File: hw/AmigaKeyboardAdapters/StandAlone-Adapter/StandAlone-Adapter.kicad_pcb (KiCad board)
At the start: 2 copper layers, 78.7 x 58.4 mm, 63 parts, among them J1 RJ10, J10 Conn_01x04, J11 Conn_01x02, J2 Conn_01x03, J3 Conn_02x03_Odd_Even, J4 Conn_01x04, J5 Conn_01x05, J6 Conn_01x03, J7 Conn_01x03, J8 Conn_01x02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

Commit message: New silkscreen (back) logo
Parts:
- added LOGO4: Stalker Logo, RetroBitLab:Stalker_16.1x17.3mm, B.Cu at (137.7, 110.8)

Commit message: First import for LCSC PCB Production and components placement
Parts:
- removed D2, D3: LED, LED_SMD:LED_1206_3216Metric_Pad1.42x1.75mm_HandSolder
- removed R2, R3: 1.5K, Resistor_SMD:R_1206_3216Metric_Pad1.30x1.75mm_HandSolder
- C1: value 10u -> 100nF; footprint Capacitor_Tantalum_SMD:CP_EIA-3216-12_Kemet-S_Pad1.58x1.35mm_HandSolder -> Capacitor_SMD:C_1206_3216Metric_Pad1.33x1.80mm_HandSolder
- C2: value 22u -> 10uF
- C7: value 4.7u -> 4.7uF
- C8, C9: value 20p -> 22pF
- D1, D4: value LED -> RED
- R1, R5: value 1.5K -> 330R
- R16, R17: value 12ohm -> 22R
- R4: value 22K -> 10K
- RESET1: footprint RetroBitLab:SW_SPST_FSMSM_3D -> RetroBitLab:SPST-7.3x3.9x2.5-WUERTH-434121025816
- USB1: value USB_A -> USB_A_SMD_LCSC; footprint RetroBitLab:CUI_UJ2-AH-4-TH -> RetroBitLab:USB_A_M04P-F000_LCSC_C386738
- XT1: footprint RetroBitLab:Crystal_HC49-4H_Vertical_3D -> Crystal:Crystal_SMD_HC49-SD
- moved LOGO3 9.19 mm to (167.9, 91.9)
- moved USB1 5.53 mm to (150.2, 83.0)
- moved C8 4.00 mm to (141.2, 87.8)
- moved C9 3.88 mm to (140.8, 100.8)
- moved XT1 1.93 mm to (135.6, 94.4)
- moved C14 1.39 mm to (157.8, 83.6)
- moved C12 1.11 mm to (159.5, 88.6)
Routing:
- net VCC3V3: track 250.0 -> 232.0 mm, vias 3 -> 1
- net KBD_CLOCK: track 66.8 -> 80.5 mm
- net NRST: track 41.7 -> 51.6 mm, vias 1 -> 0
- net VCC12V: track 8.37 -> 0.00 mm
- net KBD_DATA: track 56.9 -> 64.7 mm
- net Net-(D3-Pad2): track 6.95 -> 0.00 mm
- net Net-(R16-Pad2): track 18.8 -> 25.4 mm
- net Net-(C8-Pad1): track 21.8 -> 26.9 mm
- net Net-(R17-Pad2): track 18.3 -> 22.4 mm
- net Net-(C7-Pad1): track 14.2 -> 18.3 mm
- net Net-(D2-Pad1): track 4.03 -> 0.00 mm
- net Net-(D4-Pad1): track 16.5 -> 13.5 mm
- net Net-(C9-Pad1): track 16.3 -> 14.0 mm
- net Net-(R6-Pad1): track 46.7 -> 48.7 mm
- net +5V: track 162.8 -> 161.4 mm
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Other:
- board text added: "https://github.com/gianlucarenzi/stalker"

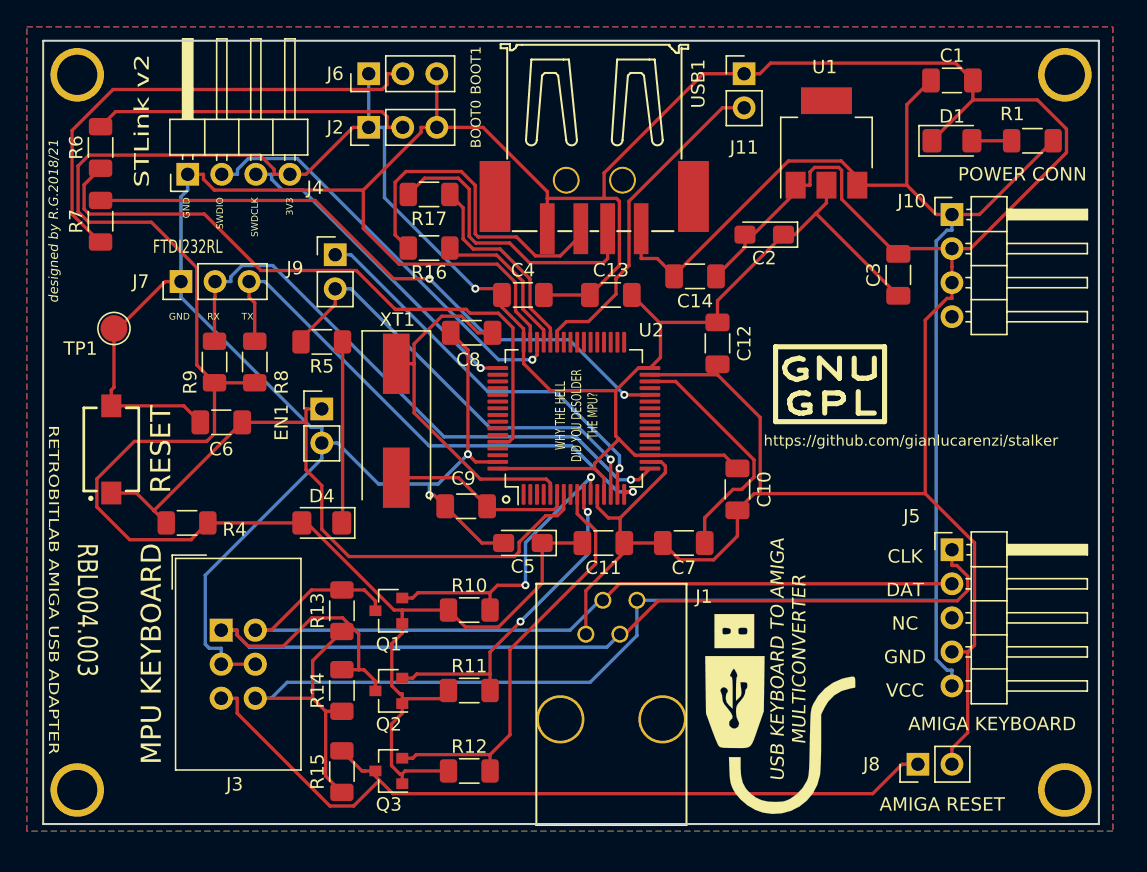
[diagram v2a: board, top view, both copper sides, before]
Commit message: All components are SMD for a easier PCB production (LCSC and others) The jumper headers are optionals, so it will be soldered if needed. The programming tool STLINK_V2 will have a special programming header male to match the connector on the board.
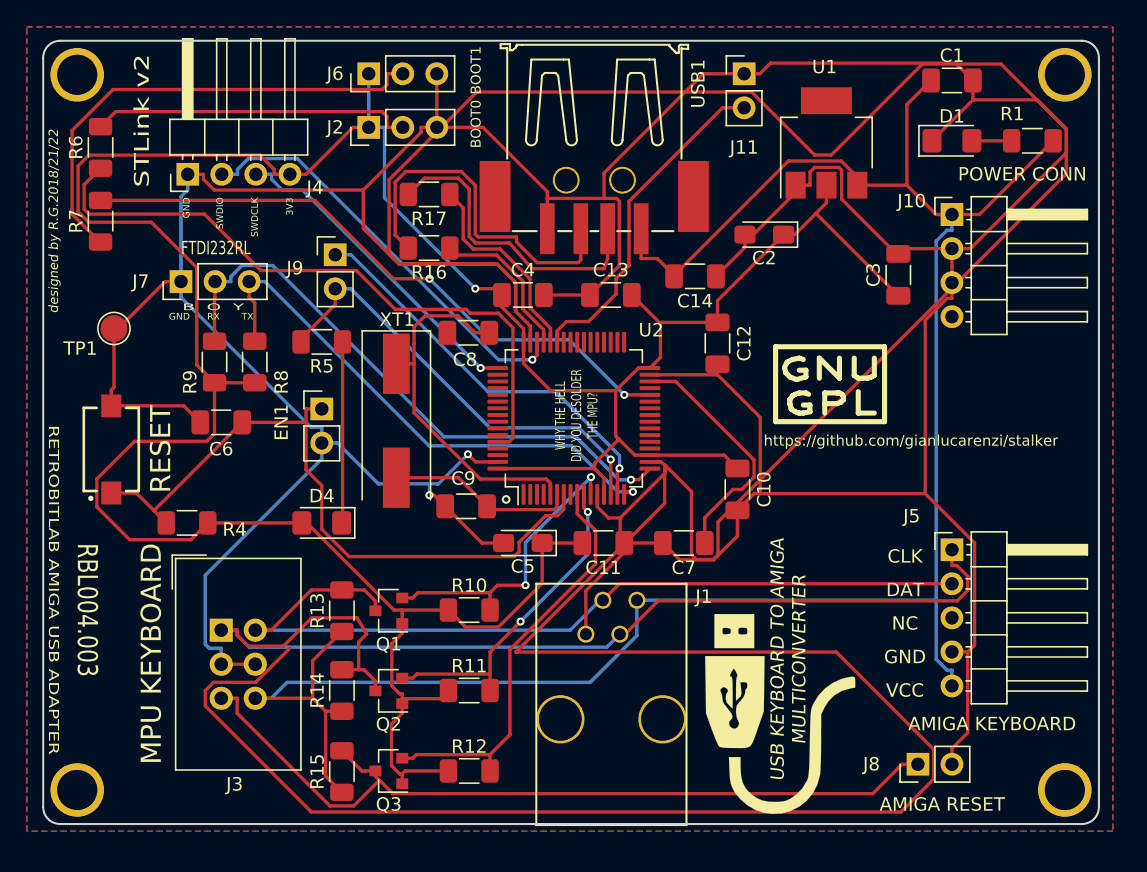
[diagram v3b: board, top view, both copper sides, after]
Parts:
- moved C8 0.25 mm to (140.9, 87.8)
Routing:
- net GND: track 368.8 -> 611.7 mm
- net Net-(R16-Pad2): track 25.4 -> 27.6 mm
- net KBD_CLOCK: track 80.5 -> 81.5 mm
- net Net-(R17-Pad2): track 22.4 -> 23.1 mm
- net Net-(C8-Pad1): track 26.9 -> 27.4 mm
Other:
- outline, holes or cut-outs redrawn
- board text added: "B O Y"
- board text added: "designed by R.G.2018/21/22"
- board text removed: "designed by R.G.2018/21"

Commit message: Sent to JLCPCB for quotes of 25 pcs and 100 pcs.
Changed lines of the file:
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@@
       (effects (font (size 0.8 0.8) (thickness 0.12)))
     )
-    (pad 1 smd roundrect (at -1.5625 0) (size 1.325 1.8) (layers F.Cu F.Paste F.Mask) (roundrect_rratio 0.1886784905660377)
+    (pad 1 smd roundrect (at -1.5625 0) (size 1.325 1.8) (layers F.Cu F.Paste F.Mask) (roundrect_rratio 0.1886777358490566)
       (net 6 +5V))
-    (pad 2 smd roundrect (at 1.5625 0) (size 1.325 1.8) (layers F.Cu F.Paste F.Mask) (roundrect_rratio 0.1886784905660377)
+    (pad 2 smd roundrect (at 1.5625 0) (size 1.325 1.8) (layers F.Cu F.Paste F.Mask) (roundrect_rratio 0.1886777358490566)
       (net 3 GND))
     (model ${KISYS3DMOD}/Capacitor_SMD.3dshapes/C_1206_3216Metric.wrl

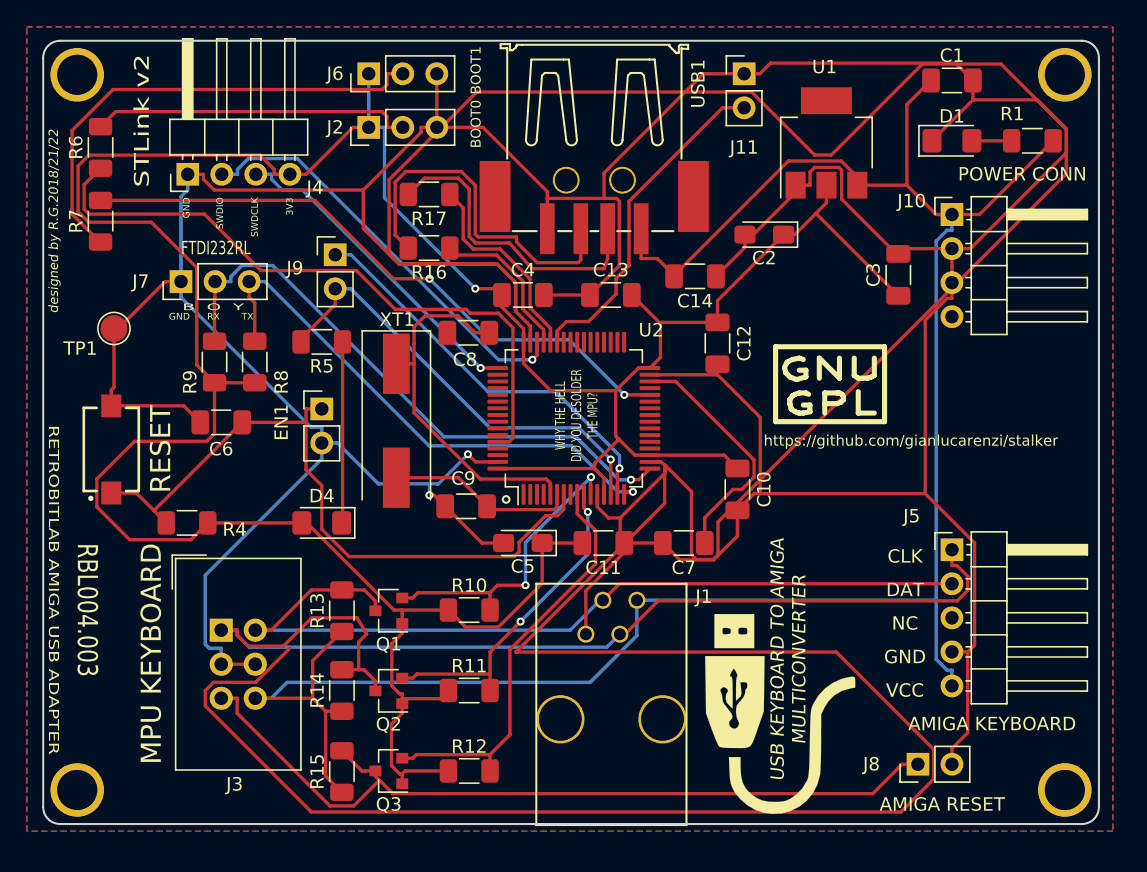
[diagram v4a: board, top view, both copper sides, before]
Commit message: Modified the JTAG STLinkV2 programmer port
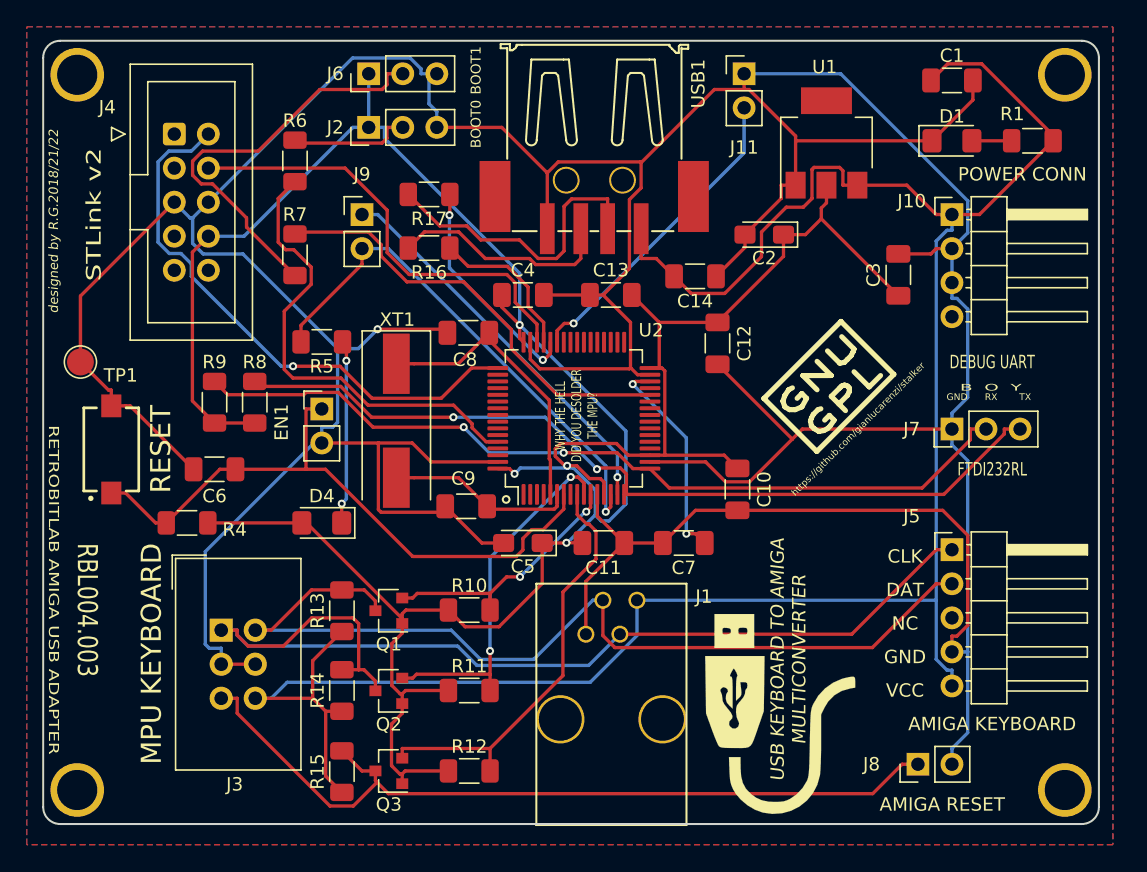
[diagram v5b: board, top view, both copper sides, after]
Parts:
- J4: value Conn_01x04 -> JTAG SWDIO SWCLK; footprint Connector_PinHeader_2.54mm:PinHeader_1x04_P2.54mm_Horizontal -> Connector_IDC:IDC-Header_2x05_P2.54mm_Vertical
- moved J7 58.5 mm to (177.0, 95.0)
- moved R7 14.7 mm to (128.0, 82.0)
- moved R6 14.5 mm to (128.0, 75.0)
- moved J9 3.61 mm to (133.0, 79.0)
- moved C6 3.54 mm to (122.0, 98.0)
- moved TP1 3.54 mm to (112.0, 90.0)
- moved J4 3.16 mm to (119.0, 73.0), turned to 0 degrees
- moved R8 3.00 mm to (125.0, 93.0)
- moved R9 3.00 mm to (122.0, 93.0)
- moved LOGO3 0.13 mm to (168.0, 92.0), turned to 45 degrees
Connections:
- J4 pad 1: GND -> Net-(J4-Pad1)
- J4 pad 2: SWDIO -> SWDCLK
- J4 pad 3: SWDCLK -> Net-(J4-Pad3)
- J4 pad 4: VCC3V3 -> SWDIO
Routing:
- net GND: track 611.7 -> 395.8 mm, vias 2 -> 1
- net UART_TX_TTL: track 40.5 -> 63.9 mm, vias 1 -> 2
- net VCC3V3: track 232.0 -> 213.1 mm, vias 1 -> 4
- net UART_RX_TTL: track 44.6 -> 63.3 mm, vias 1 -> 2
- net SWDCLK: track 24.2 -> 42.2 mm
- net BOOT0: track 24.0 -> 9.09 mm
- net Net-(R7-Pad2): track 47.0 -> 32.9 mm, vias 2 -> 0
- net Net-(R6-Pad1): track 48.7 -> 35.1 mm
- net Net-(R16-Pad2): track 27.6 -> 16.8 mm
- net +5V: track 161.4 -> 168.1 mm
- net KBD_DATA: track 64.7 -> 70.9 mm
- net Net-(C8-Pad1): track 27.4 -> 21.7 mm
- net TP1: track 33.4 -> 38.6 mm
- net BOOT1: track 36.1 -> 31.0 mm
- net NRST: track 51.6 -> 47.8 mm
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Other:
- board text added: "DEBUG UART"
- board text removed: "3V3"
- board text removed: "SWDCLK"
- board text removed: "SWDIO"
